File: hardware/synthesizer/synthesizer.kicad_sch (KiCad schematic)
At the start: 4 parts, among them J2 Input 2, J3 Input 1, J4 Output 1, J5 Output 2

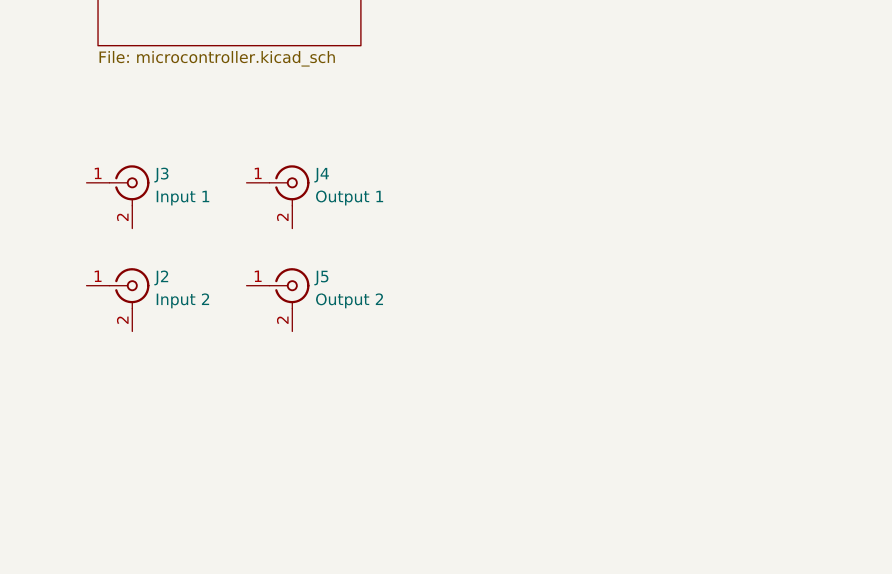
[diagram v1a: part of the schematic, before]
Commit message: add logo to every sheet
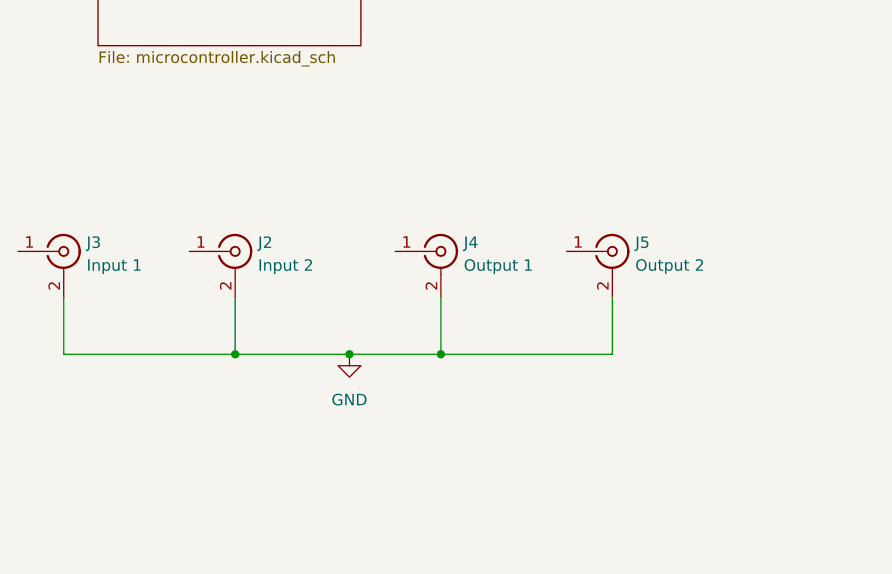
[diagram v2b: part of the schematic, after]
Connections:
- net GND: now reaches J3.2 (Ext)
- net GND: now also J2.2 (Ext), J4.2 (Ext), J5.2 (Ext)
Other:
- moved on the sheet: J2, J3, J4, J5
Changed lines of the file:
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@@
 		)
+	)
+	(junction
+		(at 73.66 166.37)
+		(diameter 0)
+		(color 0 0 0 0)
+	)
+	(junction
+		(at 83.82 166.37)
+		(diameter 0)
+		(color 0 0 0 0)
+	)
+	(junction
+		(at 60.96 166.37)
+		(diameter 0)
+		(color 0 0 0 0)
 	)
 	(wire
@@
 		)
 	)
+	(wire
+		(pts
+			(xy 73.66 166.37) (xy 83.82 166.37)
+		)
+		(stroke
+			(width 0)
+			(type default)
+		)
+	)
+	(wire
+		(pts
+			(xy 41.91 160.02) (xy 41.91 166.37)
+		)
+		(stroke
+			(width 0)
+			(type default)
+		)
+	)
+	(wire
+		(pts
+			(xy 83.82 160.02) (xy 83.82 166.37)
+		)
+		(stroke
+			(width 0)
+			(type default)
+		)
+	)
+	(wire
+		(pts
+			(xy 102.87 160.02) (xy 102.87 166.37)
+		)
+		(stroke
+			(width 0)
+			(type default)
+		)
+	)
+	(wire
+		(pts
+			(xy 60.96 160.02) (xy 60.96 166.37)
+		)
+		(stroke
+			(width 0)
+			(type default)
+		)
+	)
+	(wire
+		(pts
+			(xy 41.91 166.37) (xy 60.96 166.37)
+		)
+		(stroke
+			(width 0)
+			(type default)
+		)
+	)
+	(wire
+		(pts
+			(xy 60.96 166.37) (xy 73.66 166.37)
+		)
+		(stroke
+			(width 0)
+			(type default)
+		)
+	)
 	(bus
 		(pts
@@
 		(pts
 			(xy 74.93 74.93) (xy 110.49 74.93)
+		)
+		(stroke
+			(width 0)
+			(type default)
+		)
+	)
+	(wire
+		(pts
+			(xy 83.82 166.37) (xy 102.87 166.37)
 		)
 		(stroke
@@
 	(symbol
 		(lib_id "Connector:Conn_Coaxial")
-		(at 49.53 147.32 0)
+		(at 41.91 154.94 0)
 		(unit 1)
 		(exclude_from_sim no)
@@
 		(fields_autoplaced yes)
 		(property "Reference" "J3"
-			(at 52.07 146.3431 0)
+			(at 44.45 153.9631 0)
 			(effects
 				(font
@@
 		)
 		(property "Value" "Input 1"
-			(at 52.07 148.8831 0)
+			(at 44.45 156.5031 0)
 			(effects
 				(font
@@
 		)
 		(property "Footprint" "Connector_Coaxial:BNC_TEConnectivity_1478035_Horizontal"
-			(at 49.53 147.32 0)
+			(at 41.91 154.94 0)
 			(effects
 				(font
@@
 		)
 		(property "Datasheet" "~"
-			(at 49.53 147.32 0)
+			(at 41.91 154.94 0)
 			(effects
 				(font
@@
 		)
 		(property "Description" "coaxial connector (BNC, SMA, SMB, SMC, Cinch/RCA, LEMO, ...)"
-			(at 49.53 147.32 0)
+			(at 41.91 154.94 0)
 			(effects
 				(font
@@
 	)
 	(symbol
+		(lib_id "power:GND")
+		(at 73.66 166.37 0)
+		(unit 1)
+		(exclude_from_sim no)
+		(in_bom yes)
+		(on_board yes)
+		(dnp no)
+		(fields_autoplaced yes)
+		(property "Reference" "#PWR040"
+			(at 73.66 172.72 0)
+			(effects
+				(font
+					(size 1.27 1.27)
+				)
+				(hide yes)
+			)
+		)
+		(property "Value" "GND"
+			(at 73.66 171.45 0)
+			(effects
+				(font
+					(size 1.27 1.27)
+				)
+			)
+		)
+		(property "Footprint" ""
+			(at 73.66 166.37 0)
+			(effects
+				(font
+					(size 1.27 1.27)
+				)
+				(hide yes)
+			)
+		)
+		(property "Datasheet" ""
+			(at 73.66 166.37 0)
+			(effects
+				(font
+					(size 1.27 1.27)
+				)
+				(hide yes)
+			)
+		)
+		(property "Description" "Power symbol creates a global label with name \"GND\" , ground"
+			(at 73.66 166.37 0)
+			(effects
+				(font
+					(size 1.27 1.27)
+				)
+				(hide yes)
+			)
+		)
+		(pin "1"
+		)
+		(instances
+			(project ""
+				(path "/f8740766-88d0-4c4d-b661-742f36f22c7b"
+					(reference "#PWR040")
+					(unit 1)
+				)
+			)
+		)
+	)
+	(symbol
 		(lib_id "Connector:Conn_Coaxial")
-		(at 49.53 158.75 0)
+		(at 60.96 154.94 0)
 		(unit 1)
 		(exclude_from_sim no)
@@
 		(fields_autoplaced yes)
 		(property "Reference" "J2"
-			(at 52.07 157.7731 0)
+			(at 63.5 153.9631 0)
 			(effects
 				(font
@@
 		)
 		(property "Value" "Input 2"
-			(at 52.07 160.3131 0)
+			(at 63.5 156.5031 0)
 			(effects
 				(font
@@
 		)
 		(property "Footprint" "Connector_Coaxial:BNC_TEConnectivity_1478035_Horizontal"
-			(at 49.53 158.75 0)
+			(at 60.96 154.94 0)
 			(effects
 				(font
@@
 		)
 		(property "Datasheet" "~"
-			(at 49.53 158.75 0)
+			(at 60.96 154.94 0)
 			(effects
 				(font
@@
 		)
 		(property "Description" "coaxial connector (BNC, SMA, SMB, SMC, Cinch/RCA, LEMO, ...)"
-			(at 49.53 158.75 0)
+			(at 60.96 154.94 0)
 			(effects
 				(font
@@
 	(symbol
 		(lib_id "Connector:Conn_Coaxial")
-		(at 67.31 147.32 0)
+		(at 83.82 154.94 0)
 		(unit 1)
 		(exclude_from_sim no)
@@
 		(fields_autoplaced yes)
 		(property "Reference" "J4"
-			(at 69.85 146.3431 0)
+			(at 86.36 153.9631 0)
 			(effects
 				(font
@@
 		)
 		(property "Value" "Output 1"
-			(at 69.85 148.8831 0)
+			(at 86.36 156.5031 0)
 			(effects
 				(font
@@
 		)
 		(property "Footprint" "Connector_Coaxial:BNC_TEConnectivity_1478035_Horizontal"
-			(at 67.31 147.32 0)
+			(at 83.82 154.94 0)
 			(effects
 				(font
@@
 		)
 		(property "Datasheet" "~"
-			(at 67.31 147.32 0)
+			(at 83.82 154.94 0)
 			(effects
 				(font
@@
 		)
 		(property "Description" "coaxial connector (BNC, SMA, SMB, SMC, Cinch/RCA, LEMO, ...)"
-			(at 67.31 147.32 0)
+			(at 83.82 154.94 0)
 			(effects
 				(font
@@
 	(symbol
 		(lib_id "Connector:Conn_Coaxial")
-		(at 67.31 158.75 0)
+		(at 102.87 154.94 0)
 		(unit 1)
 		(exclude_from_sim no)
@@
 		(fields_autoplaced yes)
 		(property "Reference" "J5"
-			(at 69.85 157.7731 0)
+			(at 105.41 153.9631 0)
 			(effects
 				(font
@@
 		)
 		(property "Value" "Output 2"
-			(at 69.85 160.3131 0)
+			(at 105.41 156.5031 0)
 			(effects
 				(font
@@
 		)
 		(property "Footprint" "Connector_Coaxial:BNC_TEConnectivity_1478035_Horizontal"
-			(at 67.31 158.75 0)
+			(at 102.87 154.94 0)
 			(effects
 				(font
@@
 		)
 		(property "Datasheet" "~"
-			(at 67.31 158.75 0)
+			(at 102.87 154.94 0)
 			(effects
 				(font
@@
 		)
 		(property "Description" "coaxial connector (BNC, SMA, SMB, SMC, Cinch/RCA, LEMO, ...)"
-			(at 67.31 158.75 0)
-			(effects
-				(font
+			(at 102.87 154.94 0)
+			(effects
+				(font

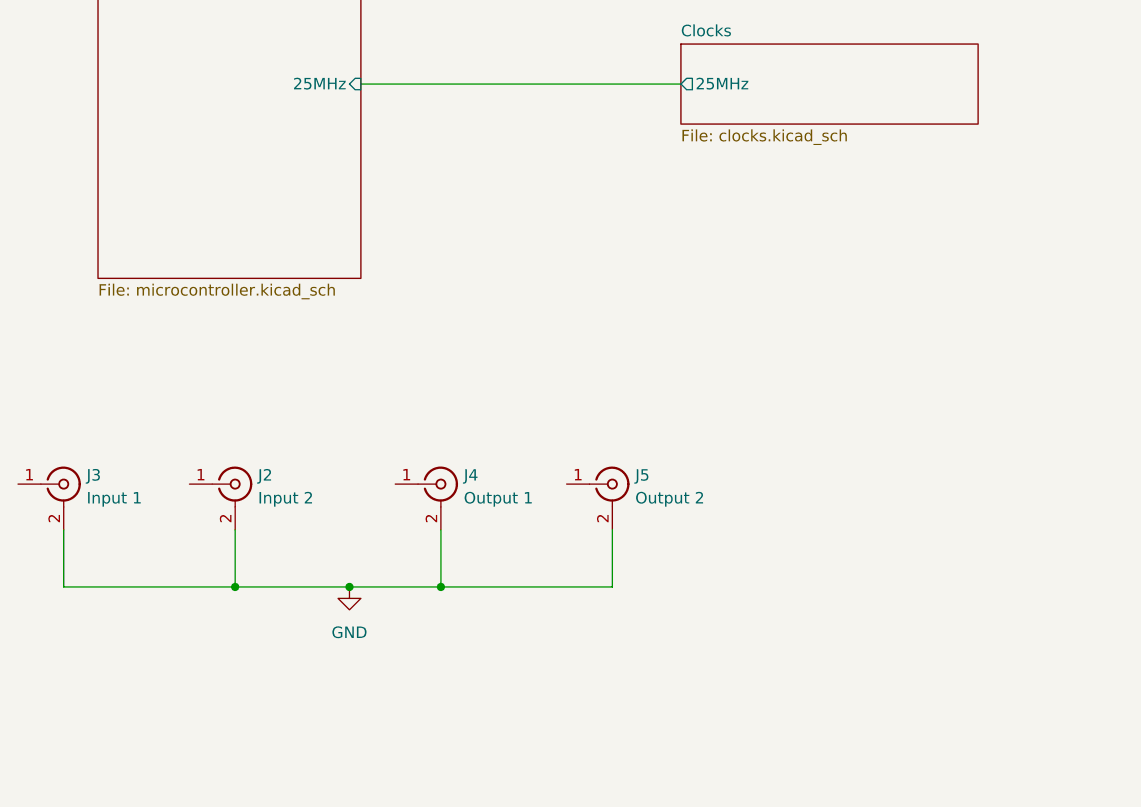
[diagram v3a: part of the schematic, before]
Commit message: add dac test
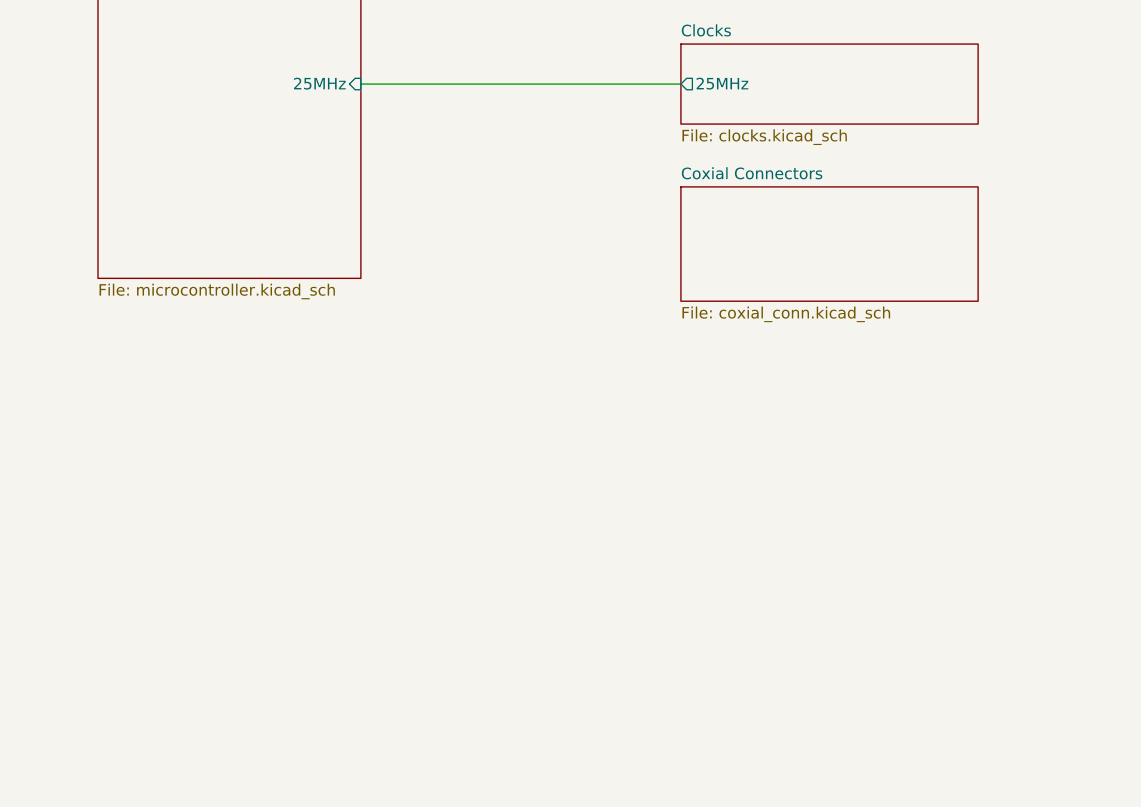
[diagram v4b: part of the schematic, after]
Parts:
- removed J2: Input 2, Connector_Coaxial:BNC_TEConnectivity_1478035_Horizontal, symbol Connector:Conn_Coaxial
- removed J3: Input 1, Connector_Coaxial:BNC_TEConnectivity_1478035_Horizontal, symbol Connector:Conn_Coaxial
- removed J4: Output 1, Connector_Coaxial:BNC_TEConnectivity_1478035_Horizontal, symbol Connector:Conn_Coaxial
- removed J5: Output 2, Connector_Coaxial:BNC_TEConnectivity_1478035_Horizontal, symbol Connector:Conn_Coaxial
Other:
- added sheet Coxial Connectors (coxial_conn.kicad_sch)
